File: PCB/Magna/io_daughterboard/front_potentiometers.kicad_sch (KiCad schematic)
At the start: 33 parts

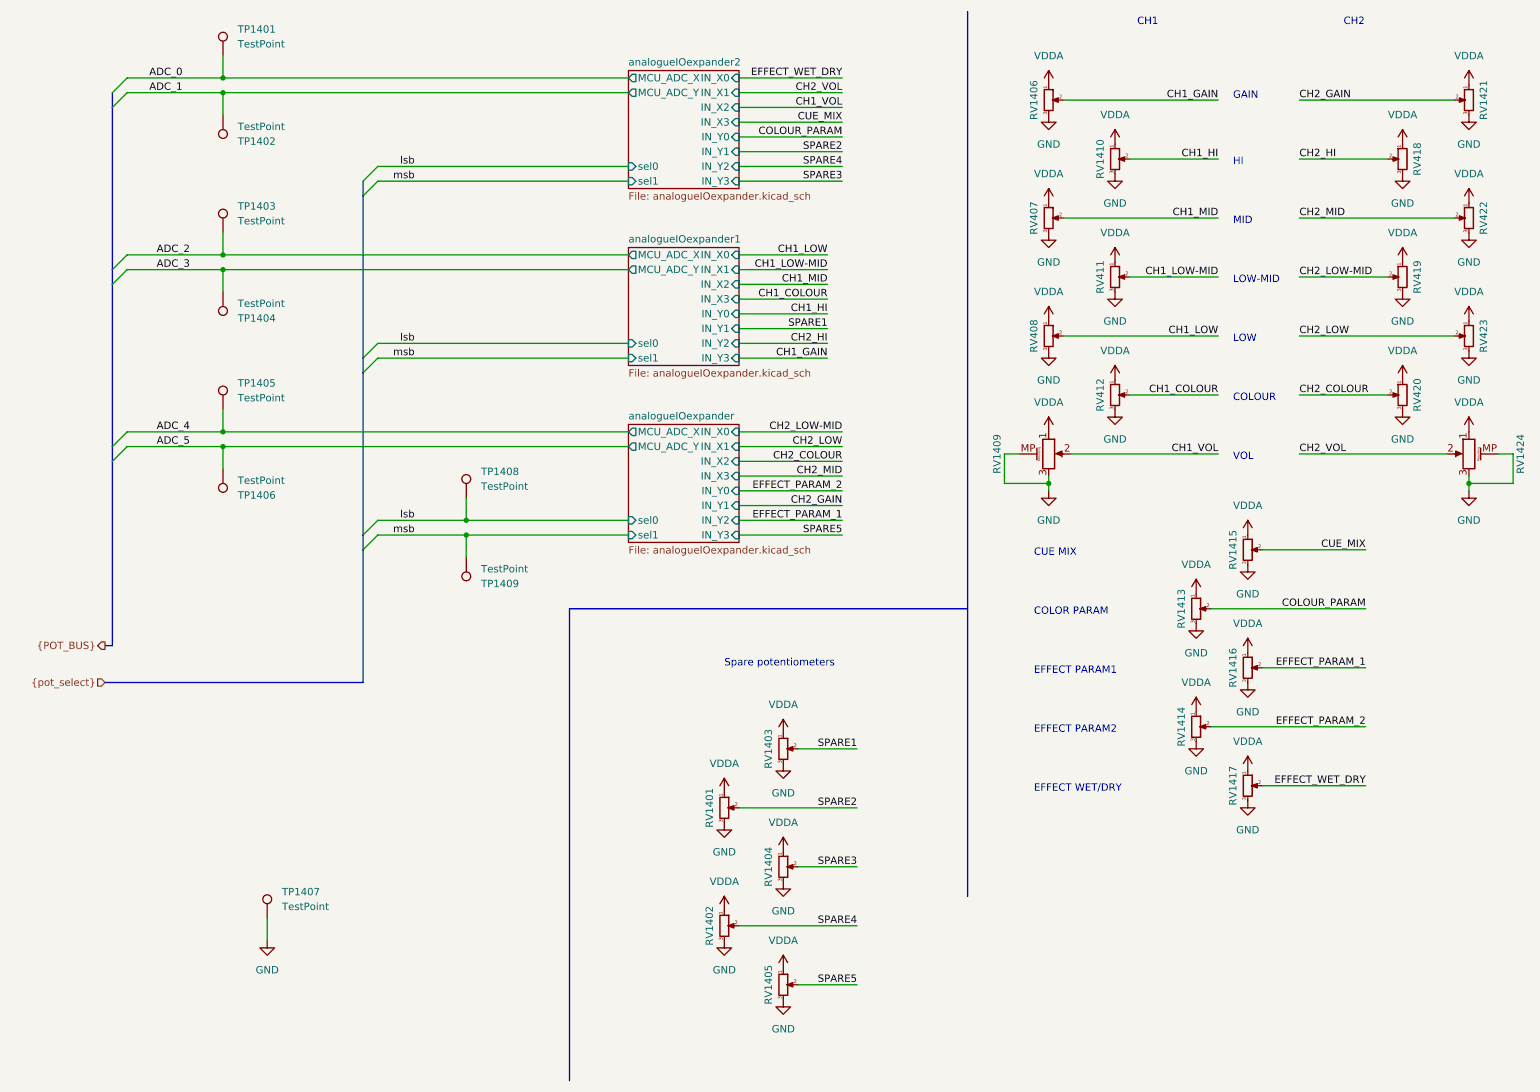
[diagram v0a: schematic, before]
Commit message: Update schematics to Kicad 9
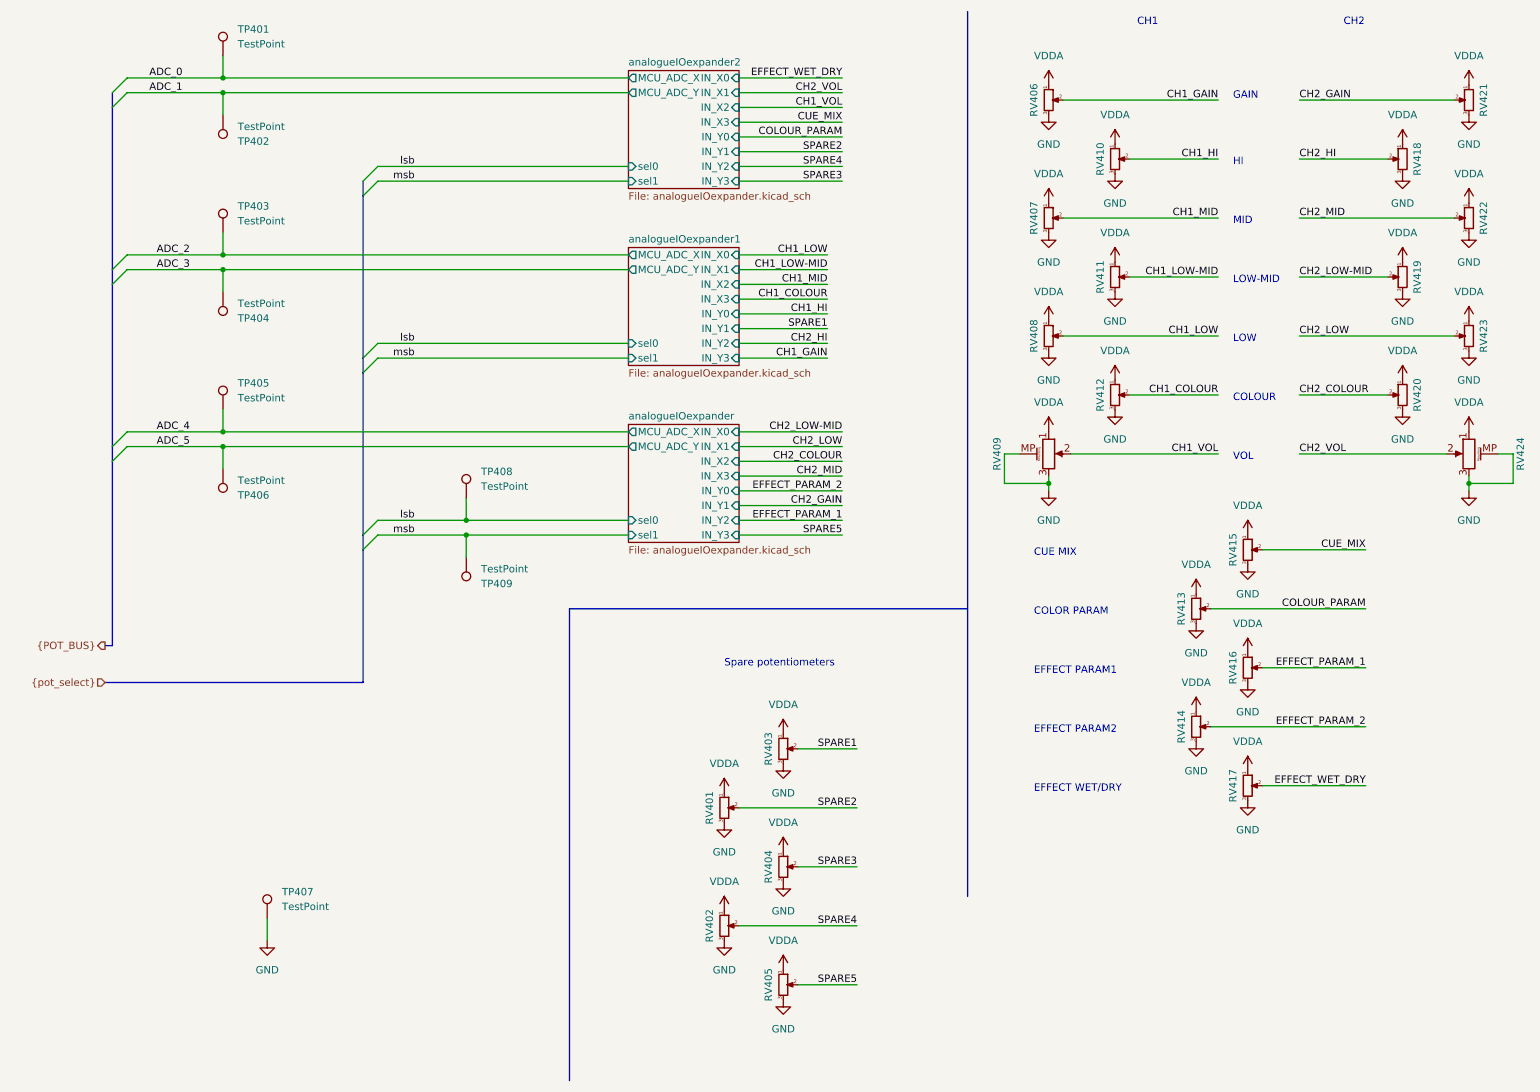
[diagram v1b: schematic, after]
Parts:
- renumbered RV1401 to RV401, RV1402 to RV402, RV1403 to RV403, RV1404 to RV404, RV1405 to RV405, RV1406 to RV406, RV1409 to RV409, RV1410 to RV410, RV1413 to RV413, RV1414 to RV414, RV1415 to RV415, RV1416 to RV416, RV1417 to RV417, RV1421 to RV421, RV1424 to RV424, TP1401 to TP401, TP1402 to TP402, TP1403 to TP403, TP1404 to TP404, TP1405 to TP405, TP1406 to TP406, TP1407 to TP407, TP1408 to TP408, TP1409 to TP409

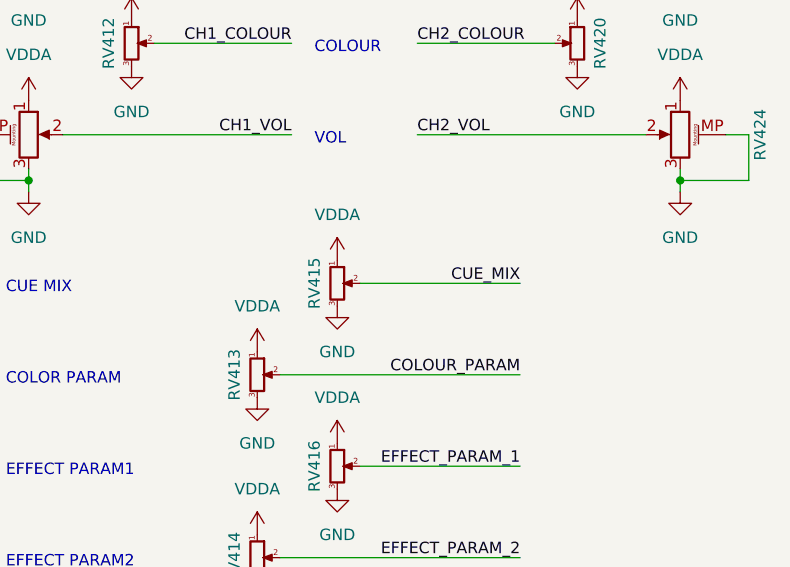
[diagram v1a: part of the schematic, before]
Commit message: Start layout and routing of Audio Daugherboard
Also a lot of small changes to everything that became apperant
when the audio daughterboard was designed. Such as the Headphone
PCB, which is now separate from the rest of the audio.
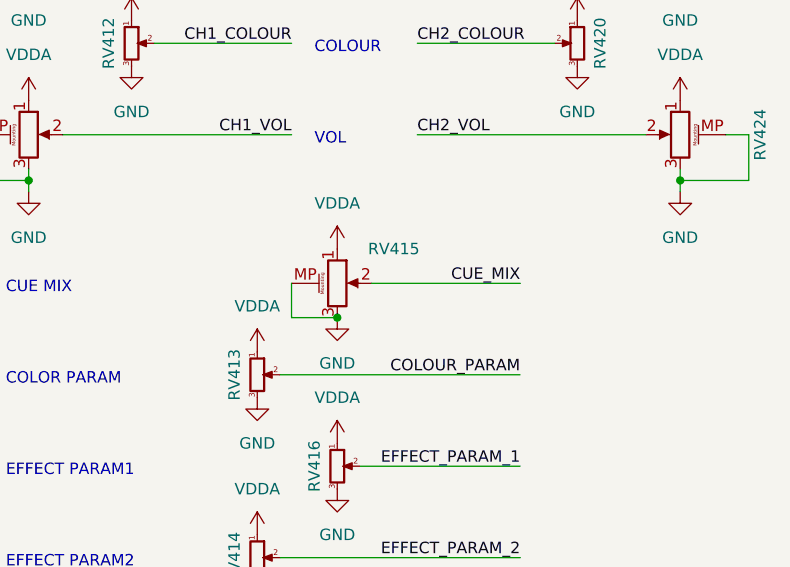
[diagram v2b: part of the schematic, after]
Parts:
- RV415: footprint Potentiometer_THT:Potentiometer_Bourns_PTV09A-2_Single_Horizontal -> Skrooter_footprints:Potentiometer_Bourns_PTV1111415AB1103; symbol Device:R_Potentiometer_Small -> Device:R_Potentiometer_MountingPin
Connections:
- net GND: now also RV415.MP (MountPin)
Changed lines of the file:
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@@
 	)
 	(junction
+		(at 226.06 109.22)
+		(diameter 0)
+		(color 0 0 0 0)
+	)
+	(junction
 		(at 49.53 87.63)
 		(diameter 0)
@@
 	(wire
 		(pts
+			(xy 220.98 105.41) (xy 220.98 109.22)
+		)
+		(stroke
+			(width 0)
+			(type default)
+		)
+	)
+	(wire
+		(pts
 			(xy 49.53 54.61) (xy 119.38 54.61)
 		)
@@
 	(wire
 		(pts
-			(xy 228.6 105.41) (xy 246.38 105.41)
+			(xy 229.87 105.41) (xy 246.38 105.41)
 		)
 		(stroke
@@
 	(wire
 		(pts
+			(xy 220.98 109.22) (xy 226.06 109.22)
+		)
+		(stroke
+			(width 0)
+			(type default)
+		)
+	)
+	(wire
+		(pts
 			(xy 138.43 36.83) (xy 156.21 36.83)
 		)
@@
 	)
 	(symbol
-		(lib_id "Device:R_Potentiometer_Small")
+		(lib_id "Device:R_Potentiometer_MountingPin")
 		(at 226.06 105.41 0)
 		(unit 1)
@@
 		(on_board yes)
 		(dnp no)
+		(fields_autoplaced yes)
 		(property "Reference" "RV415"
-			(at 223.52 105.41 90)
+			(at 232.3397 101.5877 0)
 			(effects
 				(font
@@
 			)
 		)
-		(property "Footprint" "Potentiometer_THT:Potentiometer_Bourns_PTV09A-2_Single_Horizontal"
+		(property "Footprint" "Skrooter_footprints:Potentiometer_Bourns_PTV1111415AB1103"
 			(at 226.06 105.41 0)
 			(effects
@@
 			)
 		)
-		(property "Description" "Potentiometer"
+		(property "Description" "Potentiometer with a mounting pin"
 			(at 226.06 105.41 0)
 			(effects
@@
 		(pin "3"
 		)
+		(pin "MP"
+		)
 		(instances
 			(project "Magna"
@@
 	(symbol
 		(lib_id "power:VDDA")
-		(at 226.06 102.87 0)
+		(at 226.06 101.6 0)
 		(unit 1)
 		(exclude_from_sim no)
@@
 		(fields_autoplaced yes)
 		(property "Reference" "#PWR0430"
-			(at 226.06 106.68 0)
+			(at 226.06 105.41 0)
 			(effects
 				(font
@@
 		)
 		(property "Value" "VDDA"
-			(at 226.06 97.79 0)
+			(at 226.06 96.52 0)
 			(effects
 				(font
@@
 		)
 		(property "Footprint" ""
-			(at 226.06 102.87 0)
+			(at 226.06 101.6 0)
 			(effects
 				(font
@@
 		)
 		(property "Datasheet" ""
-			(at 226.06 102.87 0)
+			(at 226.06 101.6 0)
 			(effects
 				(font
@@
 		)
 		(property "Description" "Power symbol creates a global label with name \"VDDA\""
-			(at 226.06 102.87 0)
+			(at 226.06 101.6 0)
 			(effects
 				(font
@@
 	(symbol
 		(lib_id "power:GND")
-		(at 226.06 107.95 0)
+		(at 226.06 109.22 0)
 		(unit 1)
 		(exclude_from_sim no)
@@
 		(fields_autoplaced yes)
 		(property "Reference" "#PWR0431"
-			(at 226.06 114.3 0)
+			(at 226.06 115.57 0)
 			(effects
 				(font
@@
 		)
 		(property "Value" "GND"
-			(at 226.06 113.03 0)
+			(at 226.06 114.3 0)
 			(effects
 				(font
@@
 		)
 		(property "Footprint" ""
-			(at 226.06 107.95 0)
+			(at 226.06 109.22 0)
 			(effects
 				(font
@@
 		)
 		(property "Datasheet" ""
-			(at 226.06 107.95 0)
+			(at 226.06 109.22 0)
 			(effects
 				(font
@@
 		)
 		(property "Description" "Power symbol creates a global label with name \"GND\" , ground"
-			(at 226.06 107.95 0)
+			(at 226.06 109.22 0)
 			(effects
 				(font

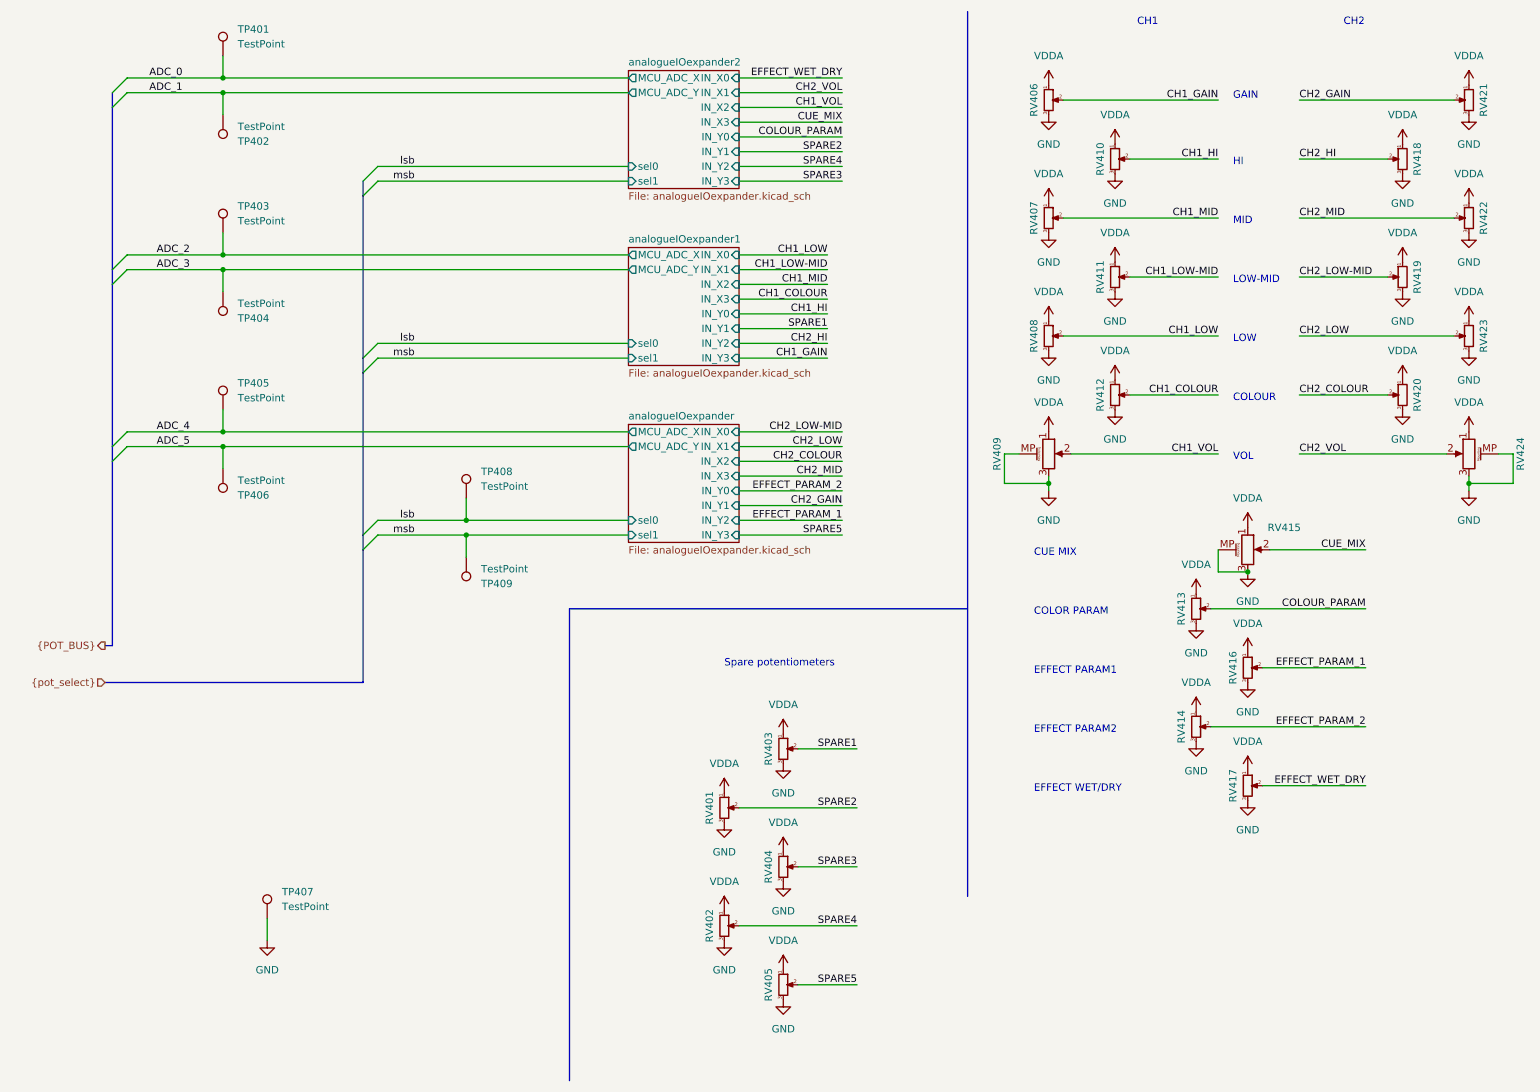
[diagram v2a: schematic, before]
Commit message: Fix board alignments and mounting holes
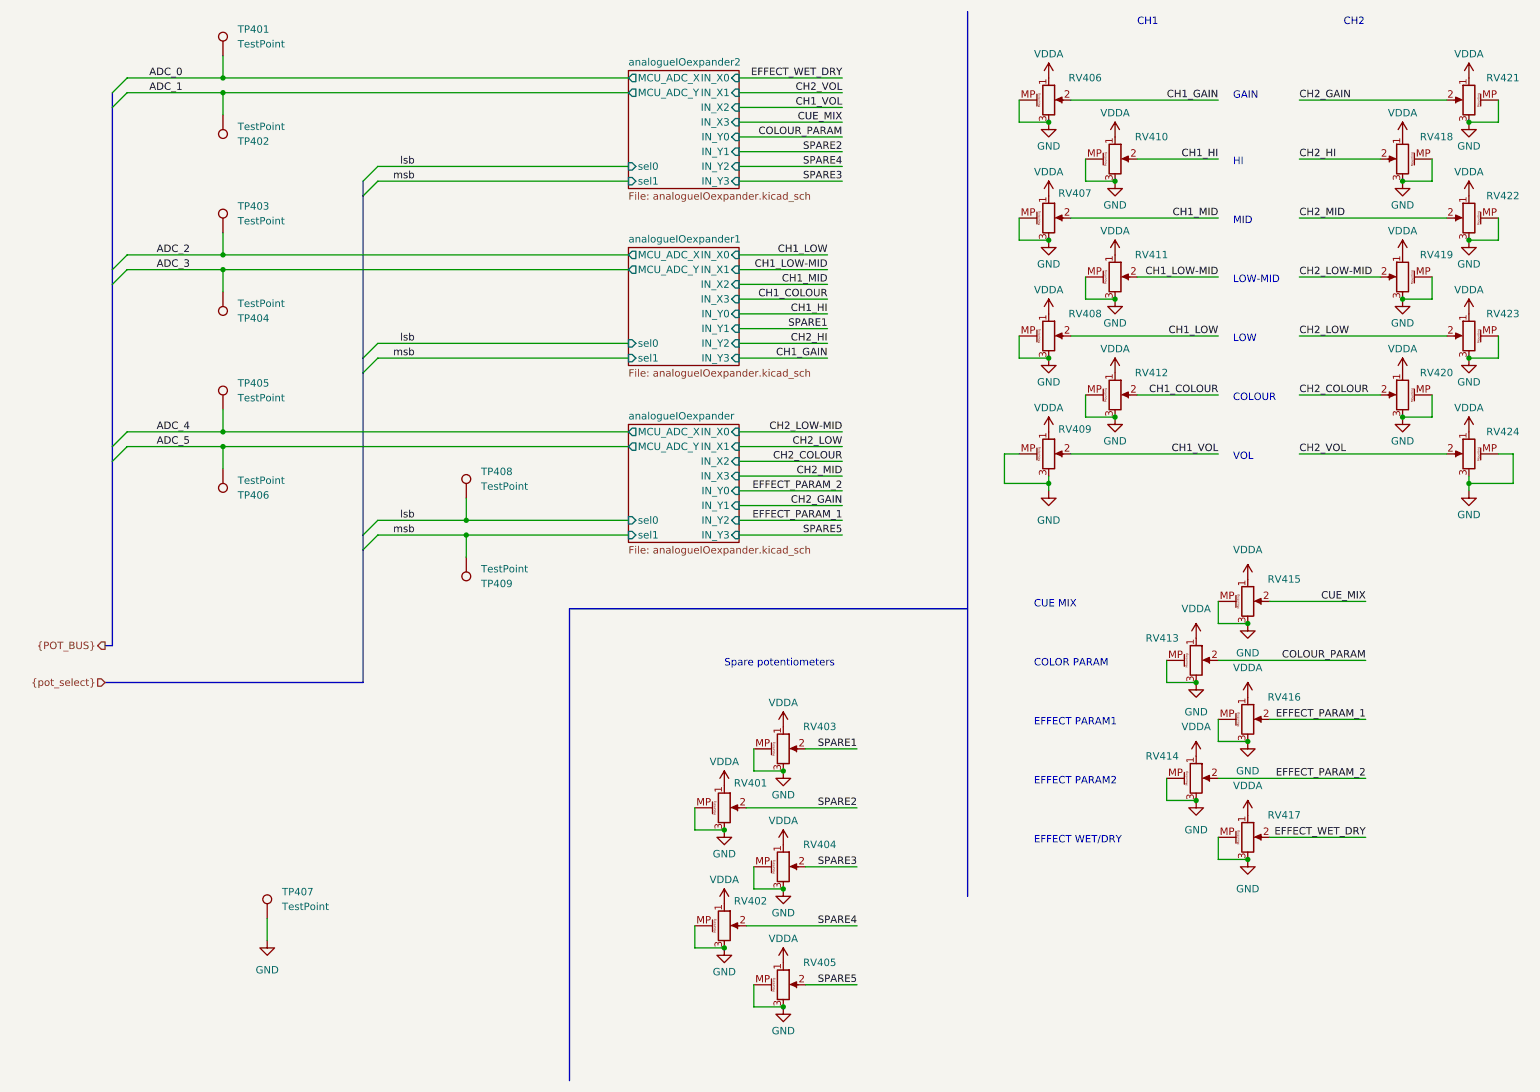
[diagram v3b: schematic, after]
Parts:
- RV401, RV402, RV403, RV404, RV405, RV406, RV407, RV408, RV410, RV411, RV412, RV413, RV414, RV416, RV417, RV418, RV419, RV420, RV421, RV422, RV423: symbol Device:R_Potentiometer_Small -> Device:R_Potentiometer_MountingPin
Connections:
- net GND: now also RV401.MP (MountPin), RV402.MP (MountPin), RV403.MP (MountPin), RV404.MP (MountPin), RV405.MP (MountPin), RV406.MP (MountPin), RV407.MP (MountPin), RV408.MP (MountPin), RV410.MP (MountPin), RV411.MP (MountPin), RV412.MP (MountPin), RV413.MP (MountPin), RV414.MP (MountPin), RV416.MP (MountPin), RV417.MP (MountPin), RV418.MP (MountPin), RV419.MP (MountPin), RV420.MP (MountPin), RV421.MP (MountPin), RV422.MP (MountPin), RV423.MP (MountPin)
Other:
- moved on the sheet: RV415
